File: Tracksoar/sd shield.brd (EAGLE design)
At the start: 43.7 x 19.6 mm, 10 parts, among them U2 HEX_CONVERTER

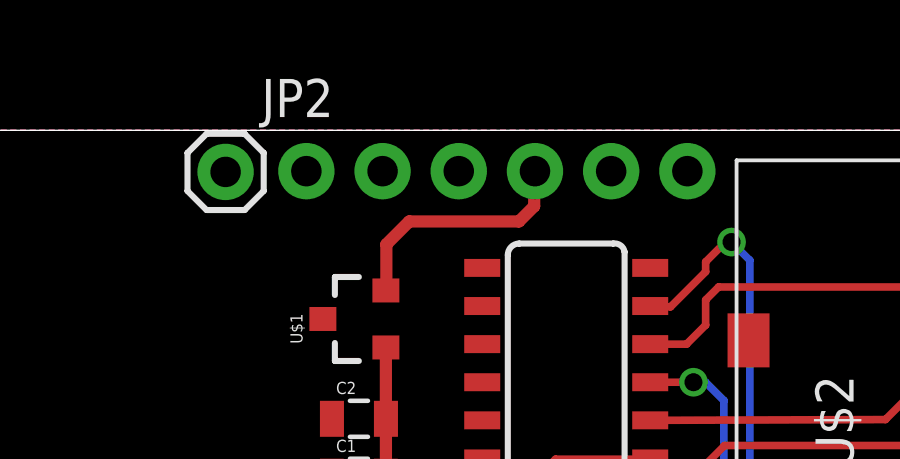
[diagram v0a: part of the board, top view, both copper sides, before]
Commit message: replace headers
replaced 2.54mm headers on all production boards with 2mm headers to
resolve daughter board issues.
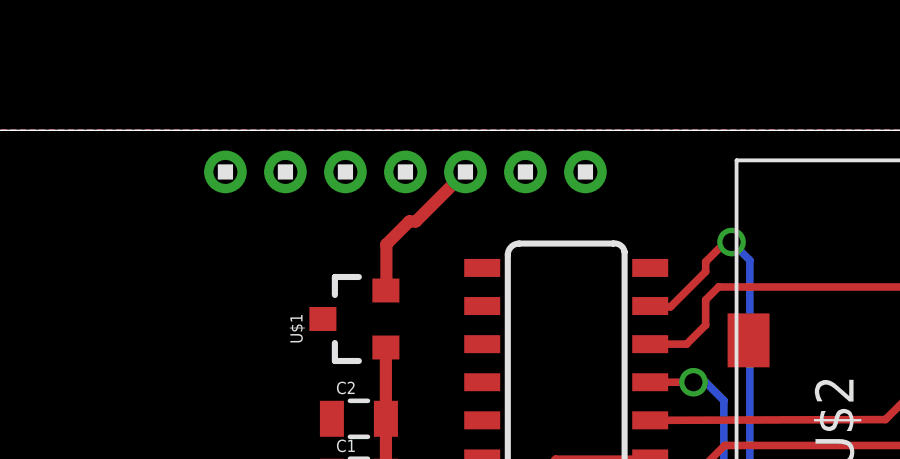
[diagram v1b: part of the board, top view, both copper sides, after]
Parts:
- removed FTDI: (no value), SparkFun-Connectors:1X06_NO_SILK
- removed JP2: (no value), SparkFun-Connectors:1X01
- added U$3: 1X7, headers(2mm):1X7
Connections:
- net !RESET: now also U$3.7; no longer JP2.1
- net DTR: now also U$3.6; no longer FTDI.1
- net GND: now also U$3.1, U$3.2; no longer FTDI.5, FTDI.6
- net RXO: now also U$3.5; no longer FTDI.2
- net TXO: now also U$3.4; no longer FTDI.3
- net VCC: now also U$3.3; no longer FTDI.4
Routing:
- net VCC: track 8.18 -> 5.18 mm
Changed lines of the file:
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@@
 </autorouter>
 <elements>
-<element name="FTDI" library="SparkFun-Connectors" package="1X06_NO_SILK" value="" x="12.9794" y="17.8562" rot="MR180">
-<attribute name="PROD_ID" value="CONN-08437" x="12.9794" y="17.8562" size="1.778" layer="28" rot="MR180" display="off"/>
-</element>
 <element name="SPI" library="SparkFun-Connectors" package="JST-4-PTH-VERT" value="" x="20.0914" y="1.651"/>
 <element name="FRAME1" library="SparkFun-Aesthetics" package="CREATIVE_COMMONS" value="FRAME-LETTER" x="14.3764" y="-8.1534"/>
 <element name="TX1" library="SparkFun-Connectors" package="JST-2-PTH-VERT" value="TX" x="14.1478" y="1.651"/>
-<element name="JP2" library="SparkFun-Connectors" package="1X01" value="" x="10.287" y="17.8308"/>
 <element name="C1" library="SparkFun-Passives" package="0805" value="10uf" x="14.732" y="7.6708"/>
 <element name="C2" library="SparkFun-Passives" package="0805" value=".1uf" x="14.732" y="9.6012"/>
@@
 </element>
 <element name="U$2" library="adafruit" package="MICROSD" value="MICROSD" x="27.2796" y="4.2164" rot="R90"/>
+<element name="U$3" library="headers(2mm)" package="1X7" value="1X7" x="16.2814" y="17.8308" rot="R180"/>
 </elements>
 <signals>
 <signal name="GND">
-<contactref element="FTDI" pad="6"/>
-<contactref element="FTDI" pad="5"/>
 <polygon width="0.4064" layer="1">
 <vertex x="-0.4064" y="19.2278"/>
@@
 <contactref element="C1" pad="1"/>
 <contactref element="C2" pad="1"/>
+<contactref element="U$3" pad="1"/>
+<contactref element="U$3" pad="2"/>
 </signal>
 <signal name="VCC">
-<contactref element="FTDI" pad="4"/>
 <contactref element="U$1" pad="2"/>
-<wire x1="20.574" y1="17.8308" x2="20.5994" y2="17.8562" width="0.254" layer="1"/>
-<wire x1="20.574" y1="17.8308" x2="20.574" y2="16.6878" width="0.4064" layer="1"/>
-<wire x1="20.574" y1="16.6878" x2="20.066" y2="16.1798" width="0.4064" layer="1"/>
-<wire x1="20.066" y1="16.1798" x2="16.4084" y2="16.1798" width="0.4064" layer="1"/>
 <wire x1="16.4084" y1="16.1798" x2="15.6464" y2="15.4178" width="0.4064" layer="1"/>
 <wire x1="15.6464" y1="15.4178" x2="15.6464" y2="13.8946" width="0.4064" layer="1"/>
 <wire x1="15.6464" y1="13.8946" x2="15.6304" y2="13.8786" width="0.4064" layer="1"/>
+<contactref element="U$3" pad="3"/>
+<wire x1="16.4084" y1="16.1798" x2="16.6304" y2="16.1798" width="0.4064" layer="1"/>
+<wire x1="16.6304" y1="16.1798" x2="18.2814" y2="17.8308" width="0.4064" layer="1"/>
 </signal>
 <signal name="DTR">
-<contactref element="FTDI" pad="1"/>
+<contactref element="U$3" pad="6"/>
 </signal>
 <signal name="RXO">
-<contactref element="FTDI" pad="2"/>
+<contactref element="U$3" pad="5"/>
 </signal>
 <signal name="TXO">
-<contactref element="FTDI" pad="3"/>
+<contactref element="U$3" pad="4"/>
 </signal>
 <signal name="MISO">
@@
 </signal>
 <signal name="!RESET">
-<contactref element="JP2" pad="1"/>
+<contactref element="U$3" pad="7"/>
 </signal>
 <signal name="3V">

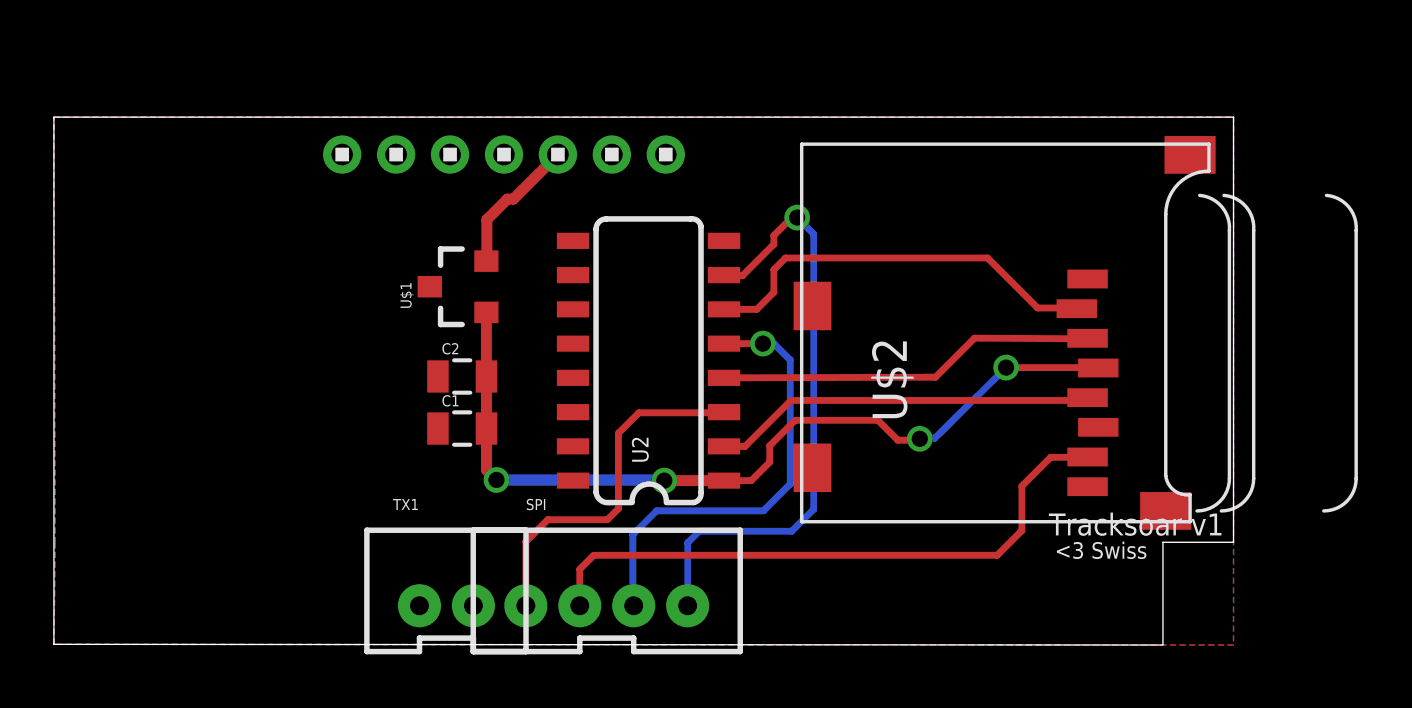
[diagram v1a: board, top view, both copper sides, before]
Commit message: mirrored sd shield
flipped components on the sd shield to be on the correct side
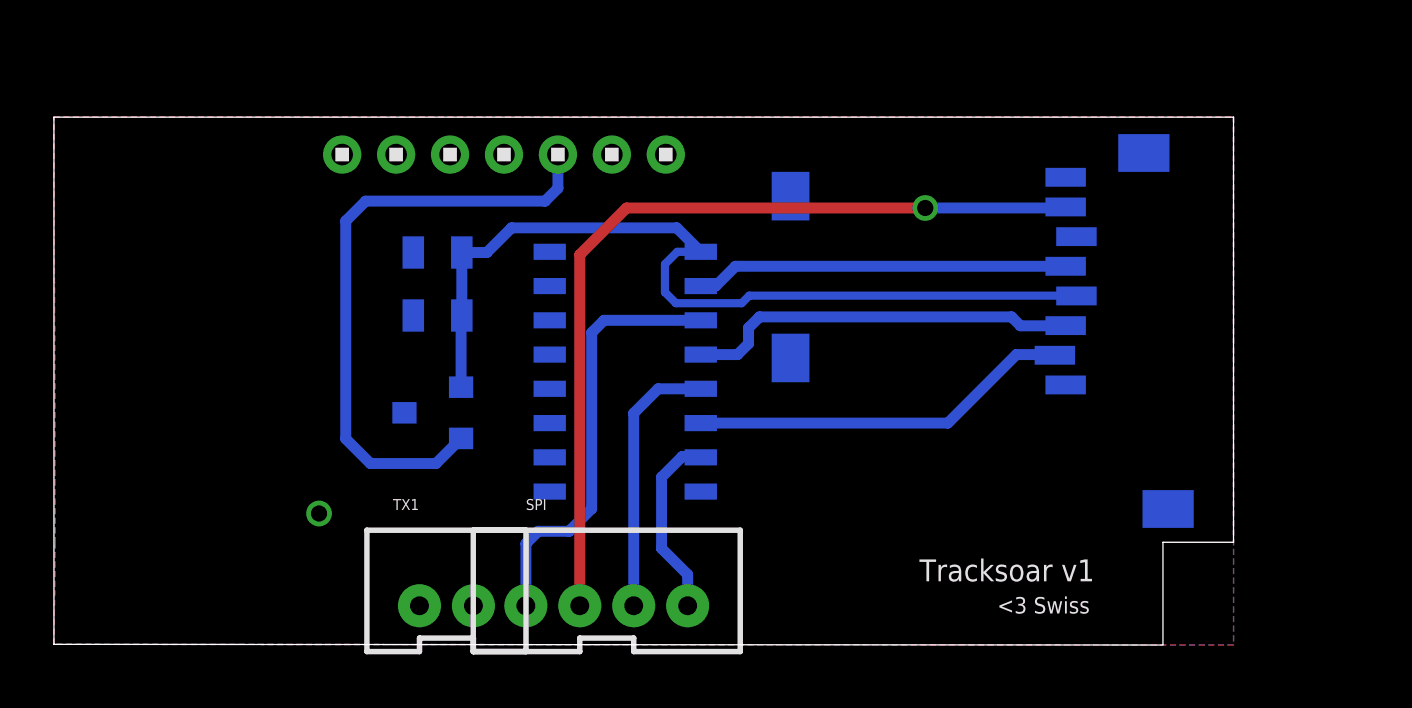
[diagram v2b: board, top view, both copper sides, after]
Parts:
- moved U$2 14.1 mm to (26.5, 18.3), flipped to the bottom, turned to 270 degrees
- moved C1 6.59 mm to (13.8, 14.2), flipped to the bottom, turned to 180 degrees
- moved U$1 4.77 mm to (13.7, 8.26), flipped to the bottom, turned to 270 degrees
- moved C2 2.44 mm to (13.8, 11.9), flipped to the bottom, turned to 180 degrees
- moved U2 0.95 mm to (20.8, 9.78), flipped to the bottom, turned to 270 degrees
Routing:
- net VCC: track 5.18 -> 22.7 mm
- net SS: track 22.4 -> 6.95 mm, vias 1 -> 0
- net MISO: track 22.9 -> 31.8 mm, vias 0 -> 1
- net MOSI: track 16.6 -> 10.00 mm, vias 1 -> 0
- net SCK: track 13.4 -> 16.0 mm
- net 3V: track 31.4 -> 32.7 mm, vias 4 -> 0
- net CS: track 15.1 -> 14.2 mm
- net DI: track 14.1 -> 14.6 mm
